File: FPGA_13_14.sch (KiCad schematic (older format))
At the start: 15 parts, among them SW1 SW_DIP_x01, U11 SN74LVC1G125DCKT, U3 S25FL128SAGMFIR01, U30 XC7A200T-FBG484

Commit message: bugs fixed
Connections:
- net labels removed: FMC1_N_LA_0, FMC1_N_LA_1, FMC1_N_LA_10, FMC1_N_LA_11, FMC1_N_LA_12, FMC1_N_LA_13, FMC1_N_LA_14, FMC1_N_LA_15, FMC1_N_LA_16, FMC1_N_LA_2, FMC1_N_LA_3, FMC1_N_LA_4, FMC1_N_LA_5, FMC1_N_LA_6, FMC1_N_LA_7, FMC1_N_LA_8, FMC1_N_LA_9, FMC1_N_LA_[0..33], FMC1_P_LA_0, FMC1_P_LA_1, FMC1_P_LA_10, FMC1_P_LA_11, FMC1_P_LA_12, FMC1_P_LA_13, FMC1_P_LA_14, FMC1_P_LA_15, FMC1_P_LA_16, FMC1_P_LA_2, FMC1_P_LA_3, FMC1_P_LA_4, FMC1_P_LA_5, FMC1_P_LA_6, FMC1_P_LA_7, FMC1_P_LA_8, FMC1_P_LA_9, FMC1_P_LA_[0..33], FMC2_N_LA_17, FMC2_N_LA_18, FMC2_N_LA_19, FMC2_N_LA_20, FMC2_N_LA_21, FMC2_N_LA_22, FMC2_N_LA_23, FMC2_N_LA_24, FMC2_N_LA_25, FMC2_N_LA_26, FMC2_N_LA_27, FMC2_N_LA_28, FMC2_N_LA_29, FMC2_N_LA_30, FMC2_N_LA_31, FMC2_N_LA_32, FMC2_N_LA_33, FMC2_N_LA_[0..33], FMC2_P_LA_17, FMC2_P_LA_18, FMC2_P_LA_19, FMC2_P_LA_20, FMC2_P_LA_21, FMC2_P_LA_22, FMC2_P_LA_23, FMC2_P_LA_24, FMC2_P_LA_25, FMC2_P_LA_26, FMC2_P_LA_27, FMC2_P_LA_28, FMC2_P_LA_29, FMC2_P_LA_30, FMC2_P_LA_31, FMC2_P_LA_32, FMC2_P_LA_33, FMC2_P_LA_[0..33]
- wire segments 187 -> 119

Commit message: bugs fixed, silkscreen edited
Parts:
- renumbered U30 to U1, U3 to U30
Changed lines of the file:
@@
 P 8500 5200
 AR Path="/5C907554/5CC902F4" Ref="U?"  Part="1"
-AR Path="/5C907554/5CC8CB69/5CC902F4" Ref="U30"  Part="1"
-F 0 "U30" H 8500 2226 50  0000 C CNN
+AR Path="/5C907554/5CC8CB69/5CC902F4" Ref="U1"  Part="1"
+F 0 "U1" H 8500 2226 50  0000 C CNN
 F 1 "XC7A200T-FBG484" H 8500 2135 50  0000 C CNN
 F 2 "ICs And Semiconductors SMD_BGA:BGA484C100P22X22_2300X2300X240" H 8500 5200 50  0001 C CNN
@@
 	7200 2300 7100 2300
 $Comp
-L AMC_FMC_Carrier-PcbDoc-rescue:S25FL128SAGMFIR01-powerMG U3
+L AMC_FMC_Carrier-PcbDoc-rescue:S25FL128SAGMFIR01-powerMG U30
 U 1 1 5C40DA57
 P 13400 850
-F 0 "U3" H 13700 1017 50  0000 C CNN
+F 0 "U30" H 13700 1017 50  0000 C CNN
 F 1 "S25FL128SAGMFIR01" H 13700 926 50  0000 C CNN
 F 2 "ICs And Semiconductors SMD:SOIC127P1030X265-16N" H 13400 850 50  0001 C CNN
@@
 $EndComp
 $Comp
-L AMC_FMC_Carrier-PcbDoc-rescue:S25FL128SAGMFIR01-powerMG U3
+L AMC_FMC_Carrier-PcbDoc-rescue:S25FL128SAGMFIR01-powerMG U30
 U 2 1 5C40DA9C
 P 14700 850
-F 0 "U3" H 15000 1017 50  0000 C CNN
+F 0 "U30" H 15000 1017 50  0000 C CNN
 F 1 "S25FL128SAGMFIR01" H 15000 926 50  0000 C CNN
 F 2 "ICs And Semiconductors SMD:SOIC127P1030X265-16N" H 14700 850 50  0001 C CNN

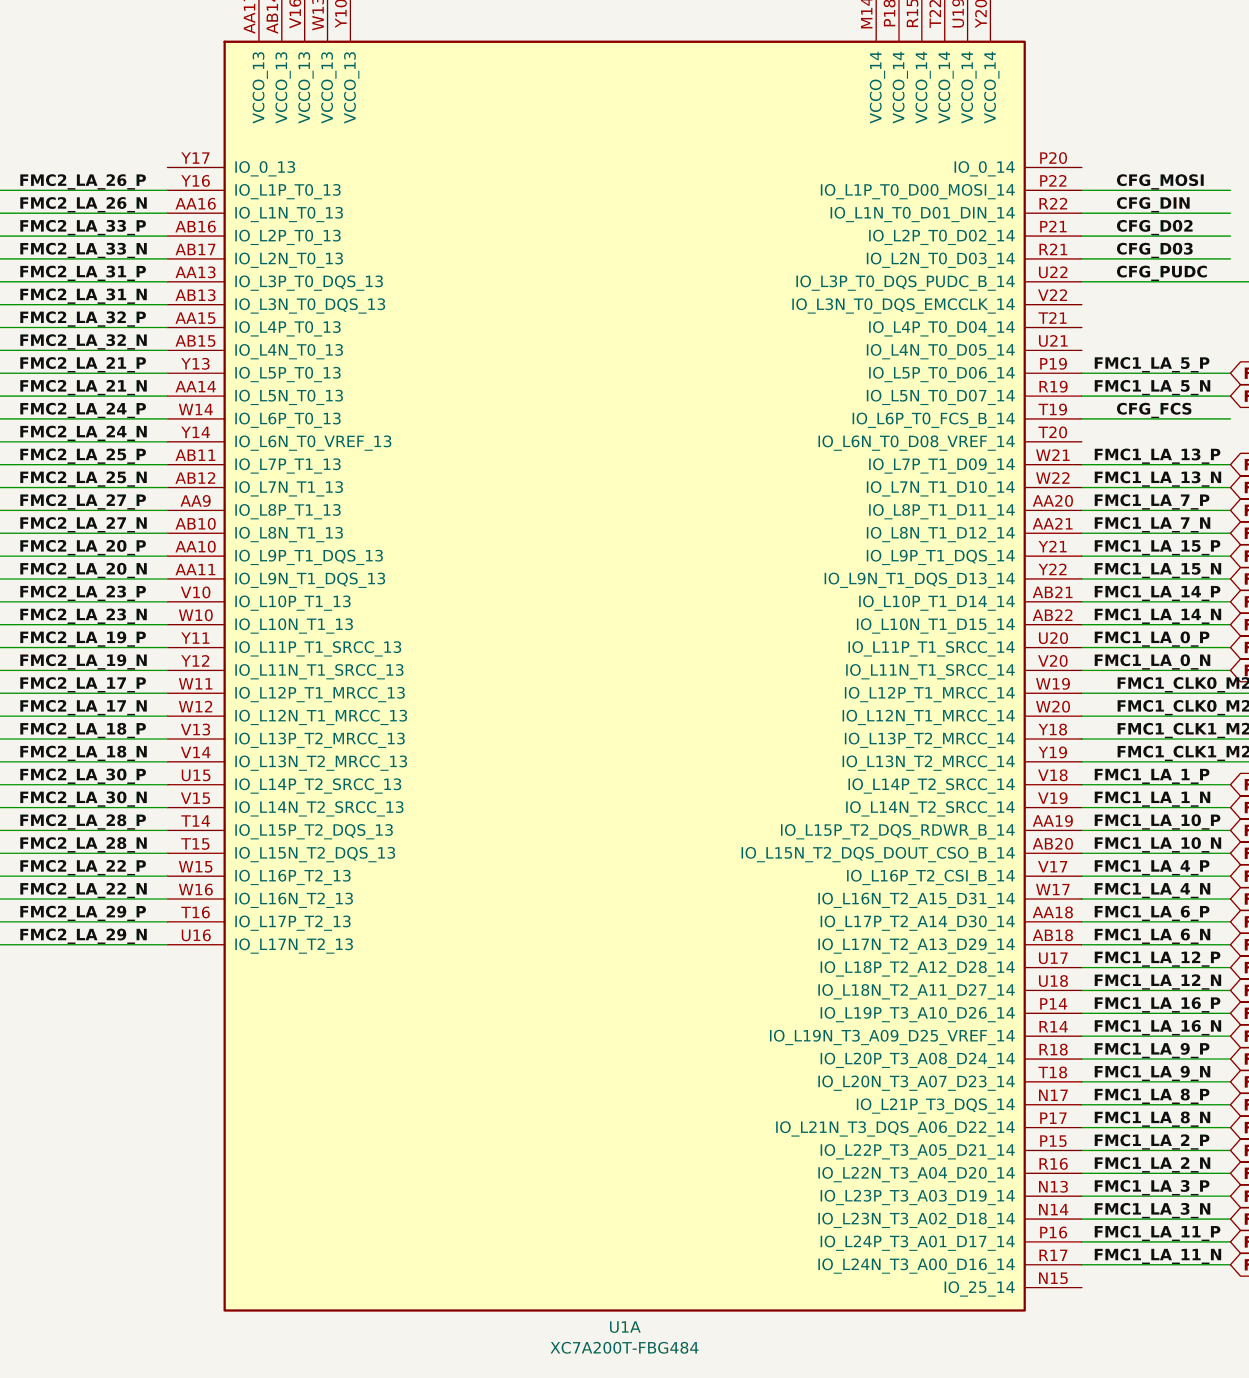
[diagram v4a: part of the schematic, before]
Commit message: new FMC JTAG chain
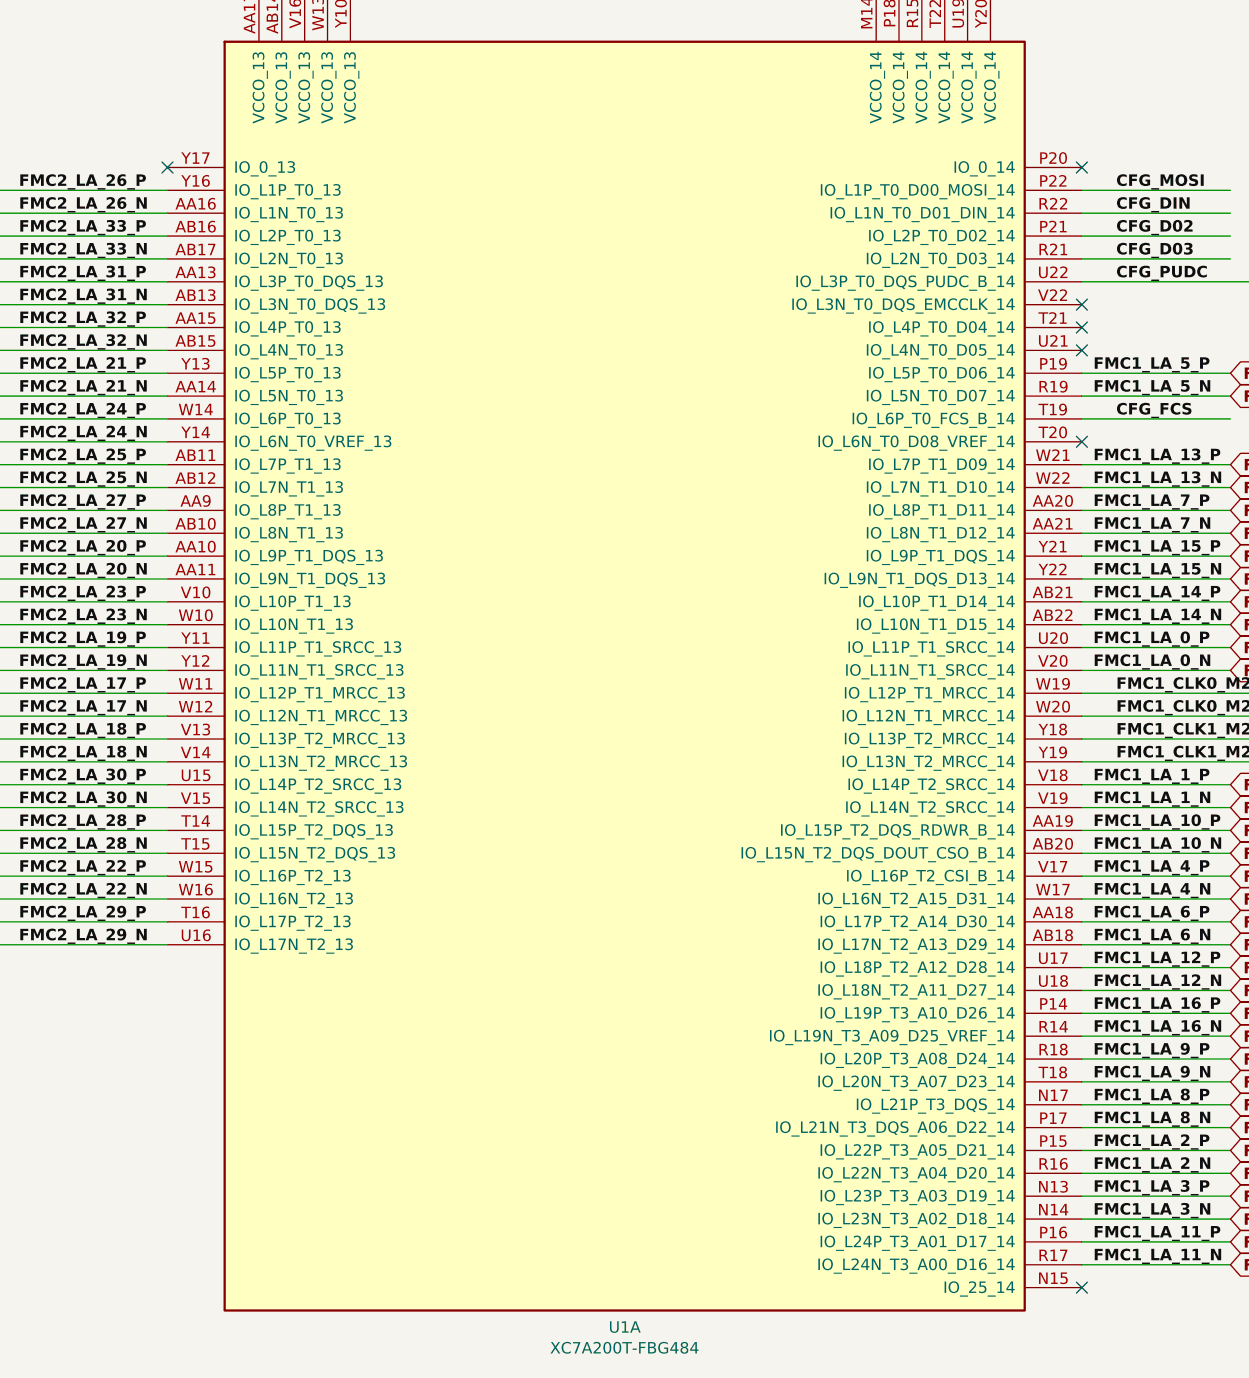
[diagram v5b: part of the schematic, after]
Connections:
- no-connect marks 7 -> 14
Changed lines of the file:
@@
 Text HLabel 11400 5400 2    50   Input ~ 10
 FMC1_CLK0_M2C_P
+NoConn ~ 10500 3100
+NoConn ~ 10500 3700
+NoConn ~ 10500 3800
+NoConn ~ 10500 3900
+NoConn ~ 10500 4300
+NoConn ~ 10500 8000
+NoConn ~ 6500 3100
 $EndSCHEMATC
